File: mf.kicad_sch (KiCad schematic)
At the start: 2 parts, among them U1 Sparkfun_Pro_Micro, U7 Sparkfun_Pro_Micro

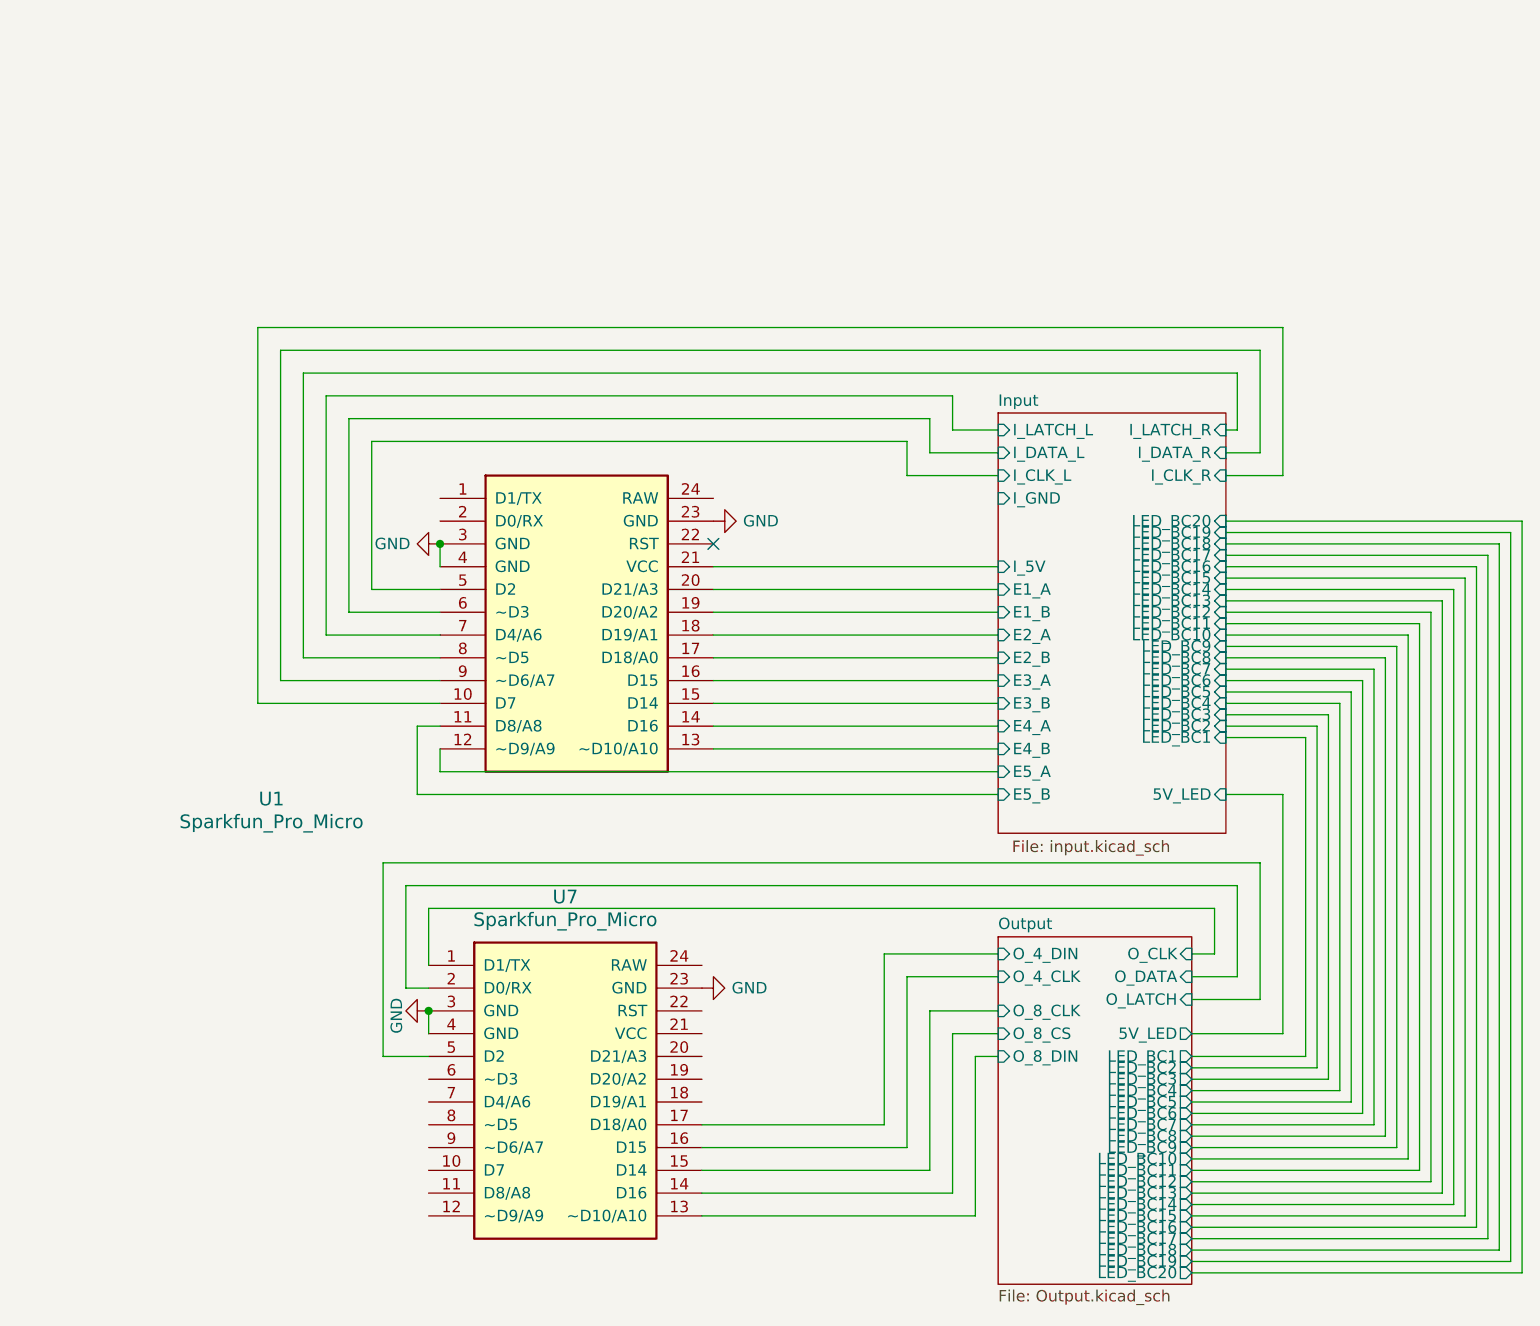
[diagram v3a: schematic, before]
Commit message: Nearly finished just need to add the footprint for the 5/6 pos switch and connect to the rest ! And it will be going into production !
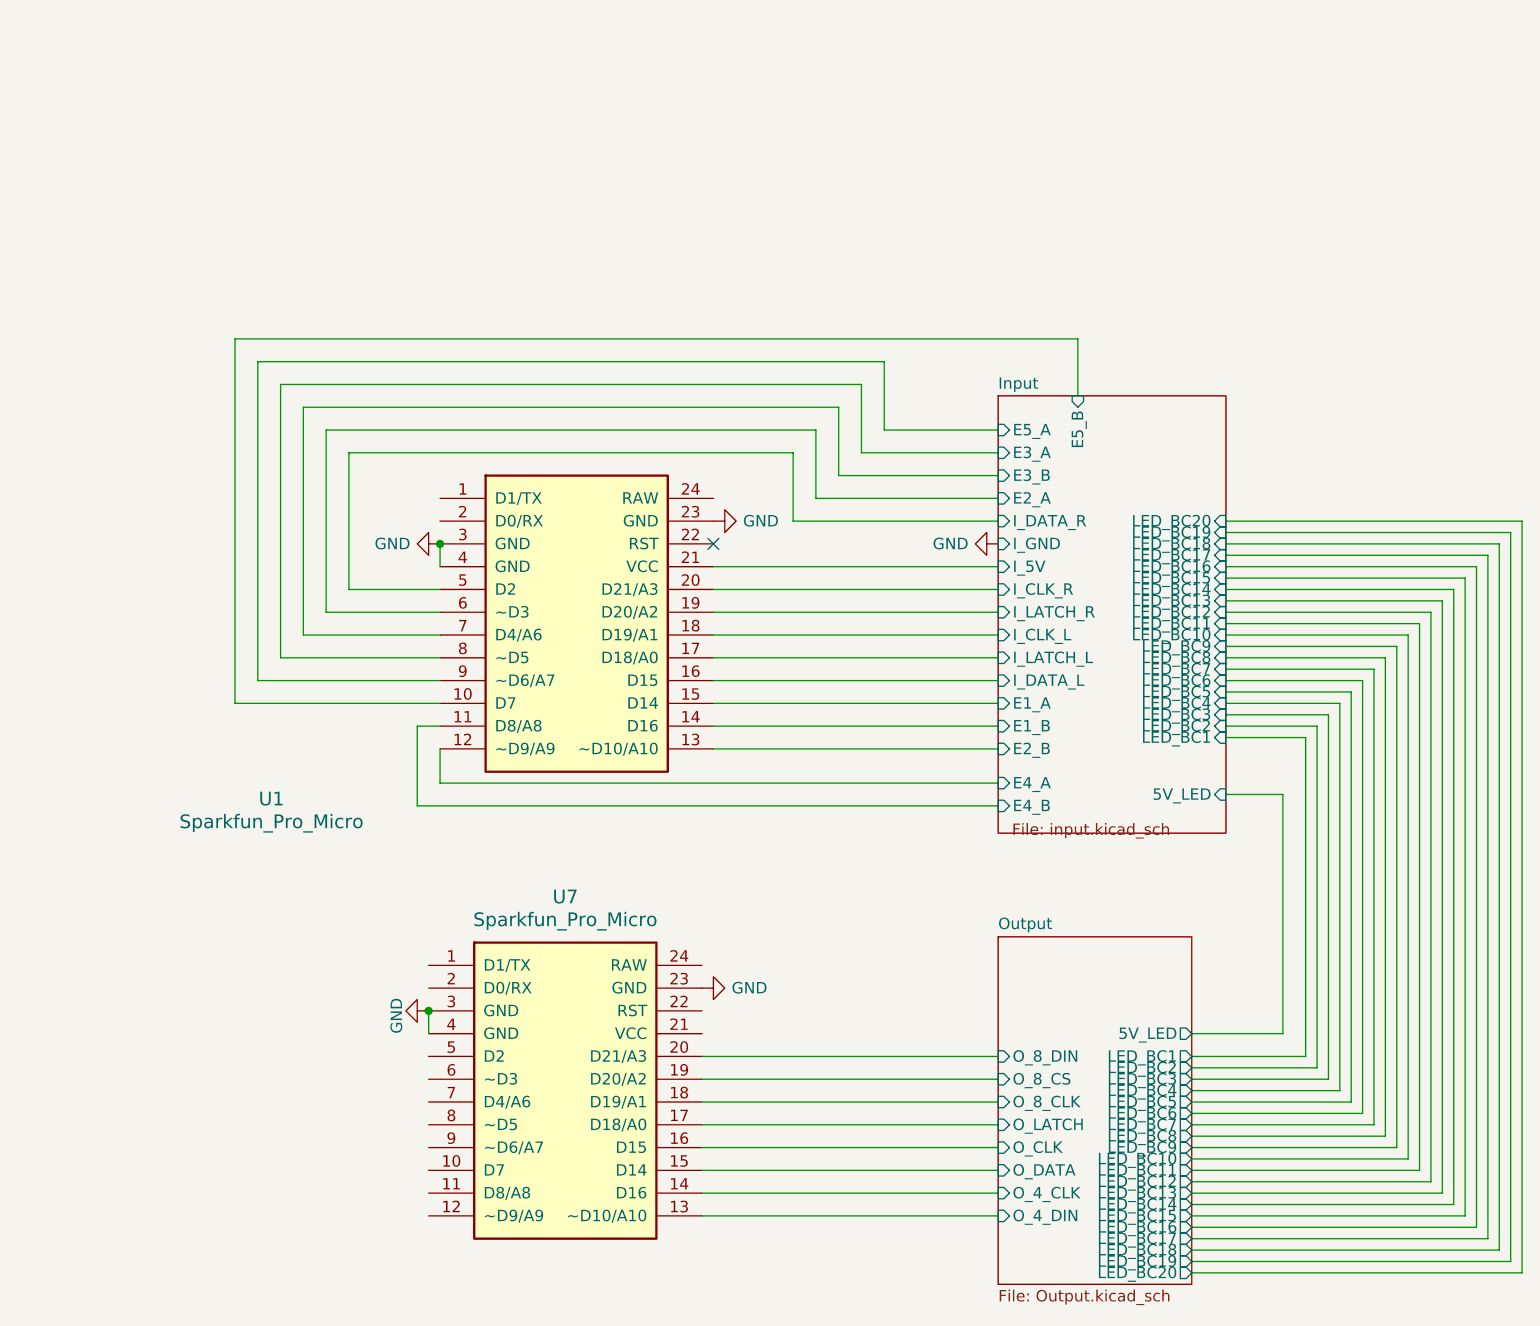
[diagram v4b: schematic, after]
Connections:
- net Input/E1_A: now also U1.15 (D14); no longer U1.20 (D21/A3)
- net Input/E1_B: now also U1.14 (D16); no longer U1.19 (D20/A2)
- net Input/E2_A: now also U1.6 (~D3); no longer U1.18 (D19/A1)
- net Input/E2_B: now also U1.13 (~D10/A10); no longer U1.17 (D18/A0)
- net Input/E3_A: now also U1.8 (~D5); no longer U1.16 (D15)
- net Input/E3_B: now also U1.7 (D4/A6); no longer U1.15 (D14)
- net Input/E4_A: now also U1.12 (~D9/A9); no longer U1.14 (D16)
- net Input/E4_B: now also U1.11 (D8/A8); no longer U1.13 (~D10/A10)
- net Input/E5_A: now also U1.9 (~D6/A7); no longer U1.12 (~D9/A9)
- net Input/E5_B: now also U1.10 (D7); no longer U1.11 (D8/A8)
- net Input/I_CLK_L: now also U1.18 (D19/A1); no longer U1.5 (D2)
- net Input/I_CLK_R: now also U1.20 (D21/A3); no longer U1.10 (D7)
- net Input/I_DATA_L: now also U1.16 (D15); no longer U1.6 (~D3)
- net Input/I_DATA_R: now also U1.5 (D2); no longer U1.9 (~D6/A7)
- net Input/I_LATCH_L: now also U1.17 (D18/A0); no longer U1.7 (D4/A6)
- net Input/I_LATCH_R: now also U1.19 (D20/A2); no longer U1.8 (~D5)
- net Output/O_4_CLK: now also U7.14 (D16); no longer U7.16 (D15)
- net Output/O_4_DIN: now also U7.13 (~D10/A10); no longer U7.17 (D18/A0)
- net Output/O_8_CLK: now also U7.18 (D19/A1); no longer U7.15 (D14)
- net Output/O_8_CS: now also U7.19 (D20/A2); no longer U7.14 (D16)
- net Output/O_8_DIN: now also U7.20 (D21/A3); no longer U7.13 (~D10/A10)
- net Output/O_CLK: now also U7.16 (D15); no longer U7.1 (D1/TX)
- net Output/O_DATA: now also U7.15 (D14); no longer U7.2 (D0/RX)
- net Output/O_LATCH: now also U7.17 (D18/A0); no longer U7.5 (D2)

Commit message: Final commit (i hope) !
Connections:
- net Output/O_4_CLK: now also U7.13 (~D10/A10); no longer U7.14 (D16)
- net Output/O_4_DIN: now also U7.14 (D16); no longer U7.13 (~D10/A10)
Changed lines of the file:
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@@
 		)
 		(pin "O_4_DIN" input
-			(at 140.97 157.48 180)
+			(at 140.97 154.94 180)
 			(effects
 				(font
@@
 		)
 		(pin "O_4_CLK" input
-			(at 140.97 154.94 180)
+			(at 140.97 157.48 180)
 			(effects
 				(font
